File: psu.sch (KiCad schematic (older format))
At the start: 26 parts, among them U2 LM5017MR, U3 TPS76333

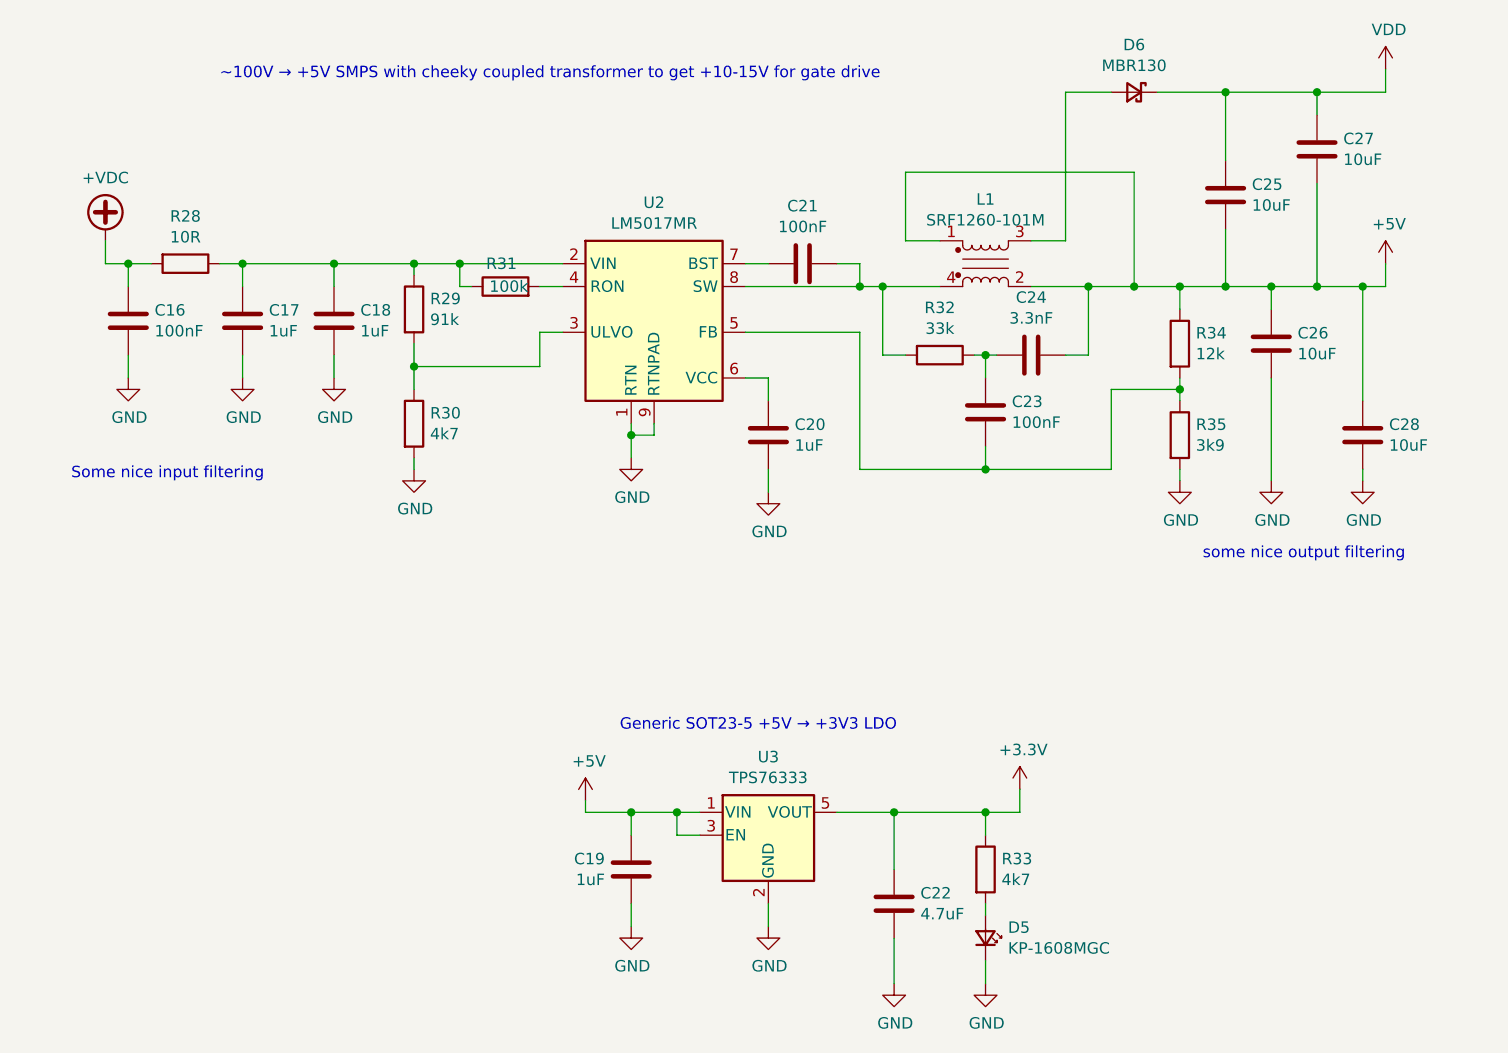
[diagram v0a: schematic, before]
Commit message: Adding some test points
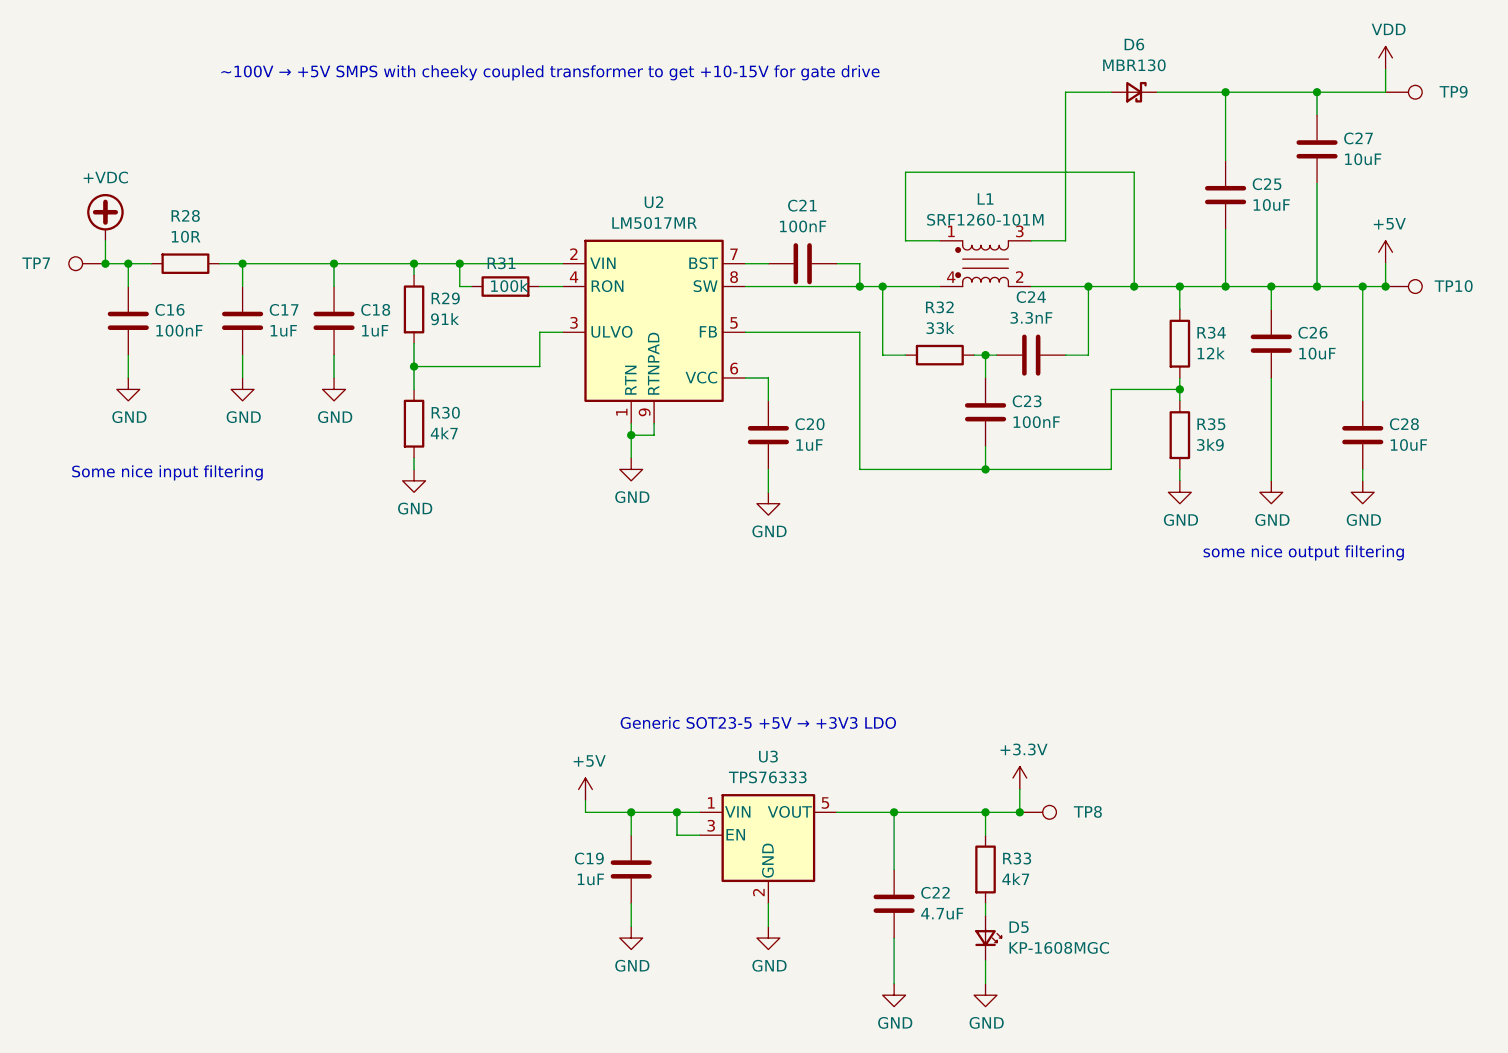
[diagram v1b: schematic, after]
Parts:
- added TP10, TP7, TP8, TP9: TestPoint, symbol Connector:TestPoint
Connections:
- net +3V3: now also TP8.1
- net +5V: now also TP10.1
- net +VDC: now also TP7.1
- net VDD: now also TP9.1
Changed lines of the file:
@@
 $EndComp
 Connection ~ 8100 2500
-Wire Wire Line
-	8100 2500 8200 2500
 Connection ~ 7900 1650
 Wire Wire Line
@@
 Wire Wire Line
 	7700 2500 7900 2500
+$Comp
+L Connector:TestPoint TP?
+U 1 1 609A4C8D
+P 8200 1650
+AR Path="/609A4C8D" Ref="TP?"  Part="1"
+AR Path="/6071142D/609A4C8D" Ref="TP9"  Part="1"
+F 0 "TP9" V 8200 1950 50  0000 C CNN
+F 1 "TestPoint" V 8304 1722 50  0001 C CNN
+F 2 "" H 8400 1650 50  0001 C CNN
+F 3 "~" H 8400 1650 50  0001 C CNN
+	1    8200 1650
+	0    1    -1   0
+$EndComp
+Wire Wire Line
+	8100 2500 8200 2500
+$Comp
+L Connector:TestPoint TP?
+U 1 1 609A7EA9
+P 8200 2500
+AR Path="/609A7EA9" Ref="TP?"  Part="1"
+AR Path="/6071142D/609A7EA9" Ref="TP10"  Part="1"
+F 0 "TP10" V 8200 2800 50  0000 C CNN
+F 1 "TestPoint" V 8304 2572 50  0001 C CNN
+F 2 "" H 8400 2500 50  0001 C CNN
+F 3 "~" H 8400 2500 50  0001 C CNN
+	1    8200 2500
+	0    1    -1   0
+$EndComp
+Connection ~ 8200 2500
+$Comp
+L Connector:TestPoint TP?
+U 1 1 609A8742
+P 6600 4800
+AR Path="/609A8742" Ref="TP?"  Part="1"
+AR Path="/6071142D/609A8742" Ref="TP8"  Part="1"
+F 0 "TP8" V 6600 5100 50  0000 C CNN
+F 1 "TestPoint" V 6704 4872 50  0001 C CNN
+F 2 "" H 6800 4800 50  0001 C CNN
+F 3 "~" H 6800 4800 50  0001 C CNN
+	1    6600 4800
+	0    1    -1   0
+$EndComp
+Connection ~ 6600 4800
+$Comp
+L Connector:TestPoint TP?
+U 1 1 609A9CC5
+P 2600 2400
+AR Path="/609A9CC5" Ref="TP?"  Part="1"
+AR Path="/6071142D/609A9CC5" Ref="TP7"  Part="1"
+F 0 "TP7" V 2600 2700 50  0000 C CNN
+F 1 "TestPoint" V 2704 2472 50  0001 C CNN
+F 2 "" H 2800 2400 50  0001 C CNN
+F 3 "~" H 2800 2400 50  0001 C CNN
+	1    2600 2400
+	0    -1   -1   0
+$EndComp
+Connection ~ 2600 2400
 $EndSCHEMATC

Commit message: Assigned all footprints
Began initial placement
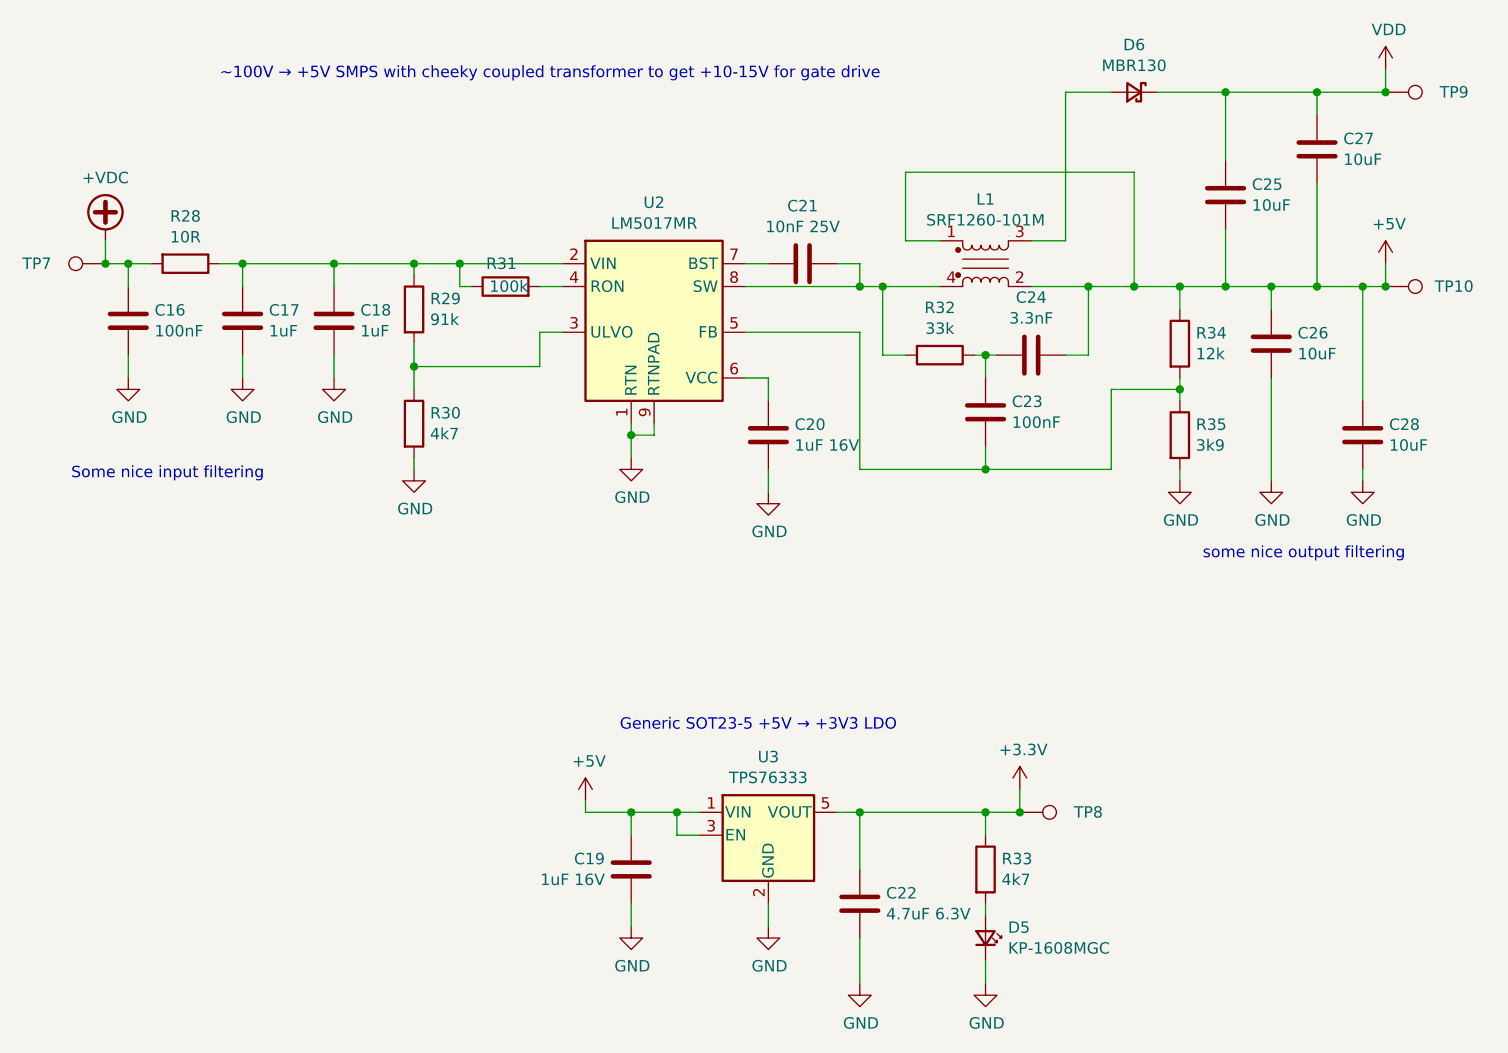
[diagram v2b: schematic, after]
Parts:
- C16: footprint (none) -> Capacitor_SMD:C_0805_2012Metric
- C17, C18, C25, C26, C27, C28: footprint (none) -> Capacitor_SMD:C_1206_3216Metric
- C19, C20: value 1uF -> 1uF 16V; footprint (none) -> Capacitor_SMD:C_0603_1608Metric
- C21: value 100nF -> 10nF 25V; footprint (none) -> Capacitor_SMD:C_0603_1608Metric
- C22: value 4.7uF -> 4.7uF 6.3V; footprint Capacitor_SMD:C_0603_1608Metric -> Capacitor_SMD:C_0805_2012Metric
- C23, C24: footprint (none) -> Capacitor_SMD:C_0402_1005Metric
- R28: footprint (none) -> Resistor_SMD:R_0603_1608Metric
- R32: footprint (none) -> Resistor_SMD:R_0402_1005Metric
- TP10, TP7, TP8, TP9: footprint (none) -> TestPoint:TestPoint_Pad_D1.5mm
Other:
- moved on the sheet: C22
